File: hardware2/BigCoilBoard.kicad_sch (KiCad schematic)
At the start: 138 parts, among them J1 Conn_01x02, J10 PFC_OUT, J11 THERM2_IN, J12 THERM3_IN, J13 THERM4_IN, J14 THERM5_IN, J15 Conn_01x03, J16 Conn_ARM_JTAG_SWD_10, J17 Conn_01x04, J18 Conn_01x04, J19 Conn_01x04, J2 Conn_01x02, J20 Screw_Terminal_01x01, J21 Screw_Terminal_01x01, J22 Screw_Terminal_01x01, J23 Screw_Terminal_01x01, J3 Conn_01x03_Pin, J5 THERM1_IN, J6 Conn_01x03_Pin, J7 Conn_01x04, J8 CONTACTOR_1, J9 CONTACTOR_2, K1 G5NB-1A-DC24, K2 G5NB-1A-DC24, Q1 T2N7002AK, Q2 T2N7002AK, Q3 T2N7002AK, Q4 T2N7002AK, Q5 T2N7002AK, Q6 T2N7002AK, Q7 T2N7002AK, U1 STM32G474CBTx, U10 IF-D95, U11 IF-E96E, U12 LD1117S33TR_SOT223, U13 TC7662Bx0A, U14 L7812, U2 MCP6477-E/SN, U3 CSTNE8M00G550000R0, U4 MCP3208, U6 MGJ2D241709SC, U7 STGAP2SM, U8 SN74LV1T34DBV, U9 IF-D95

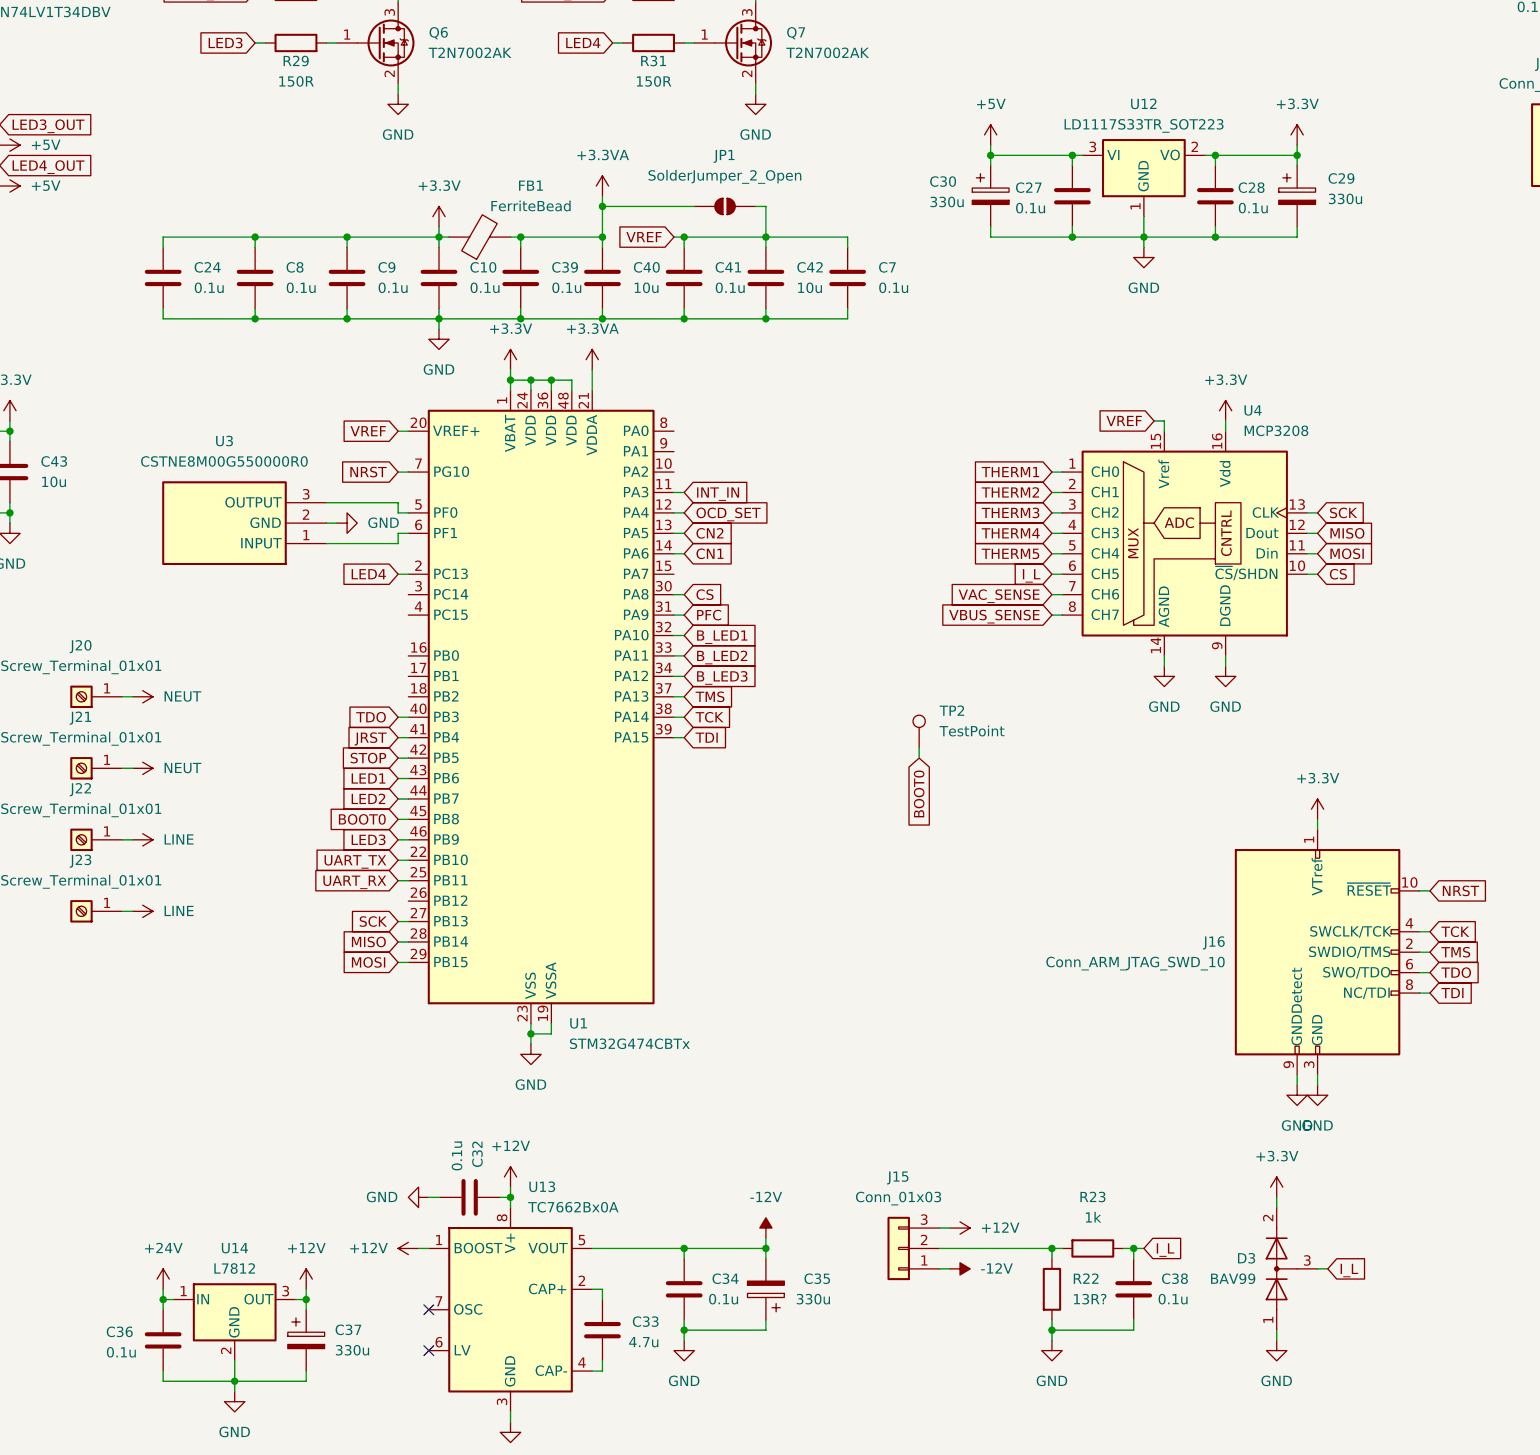
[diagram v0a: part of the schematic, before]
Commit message: back to int adc
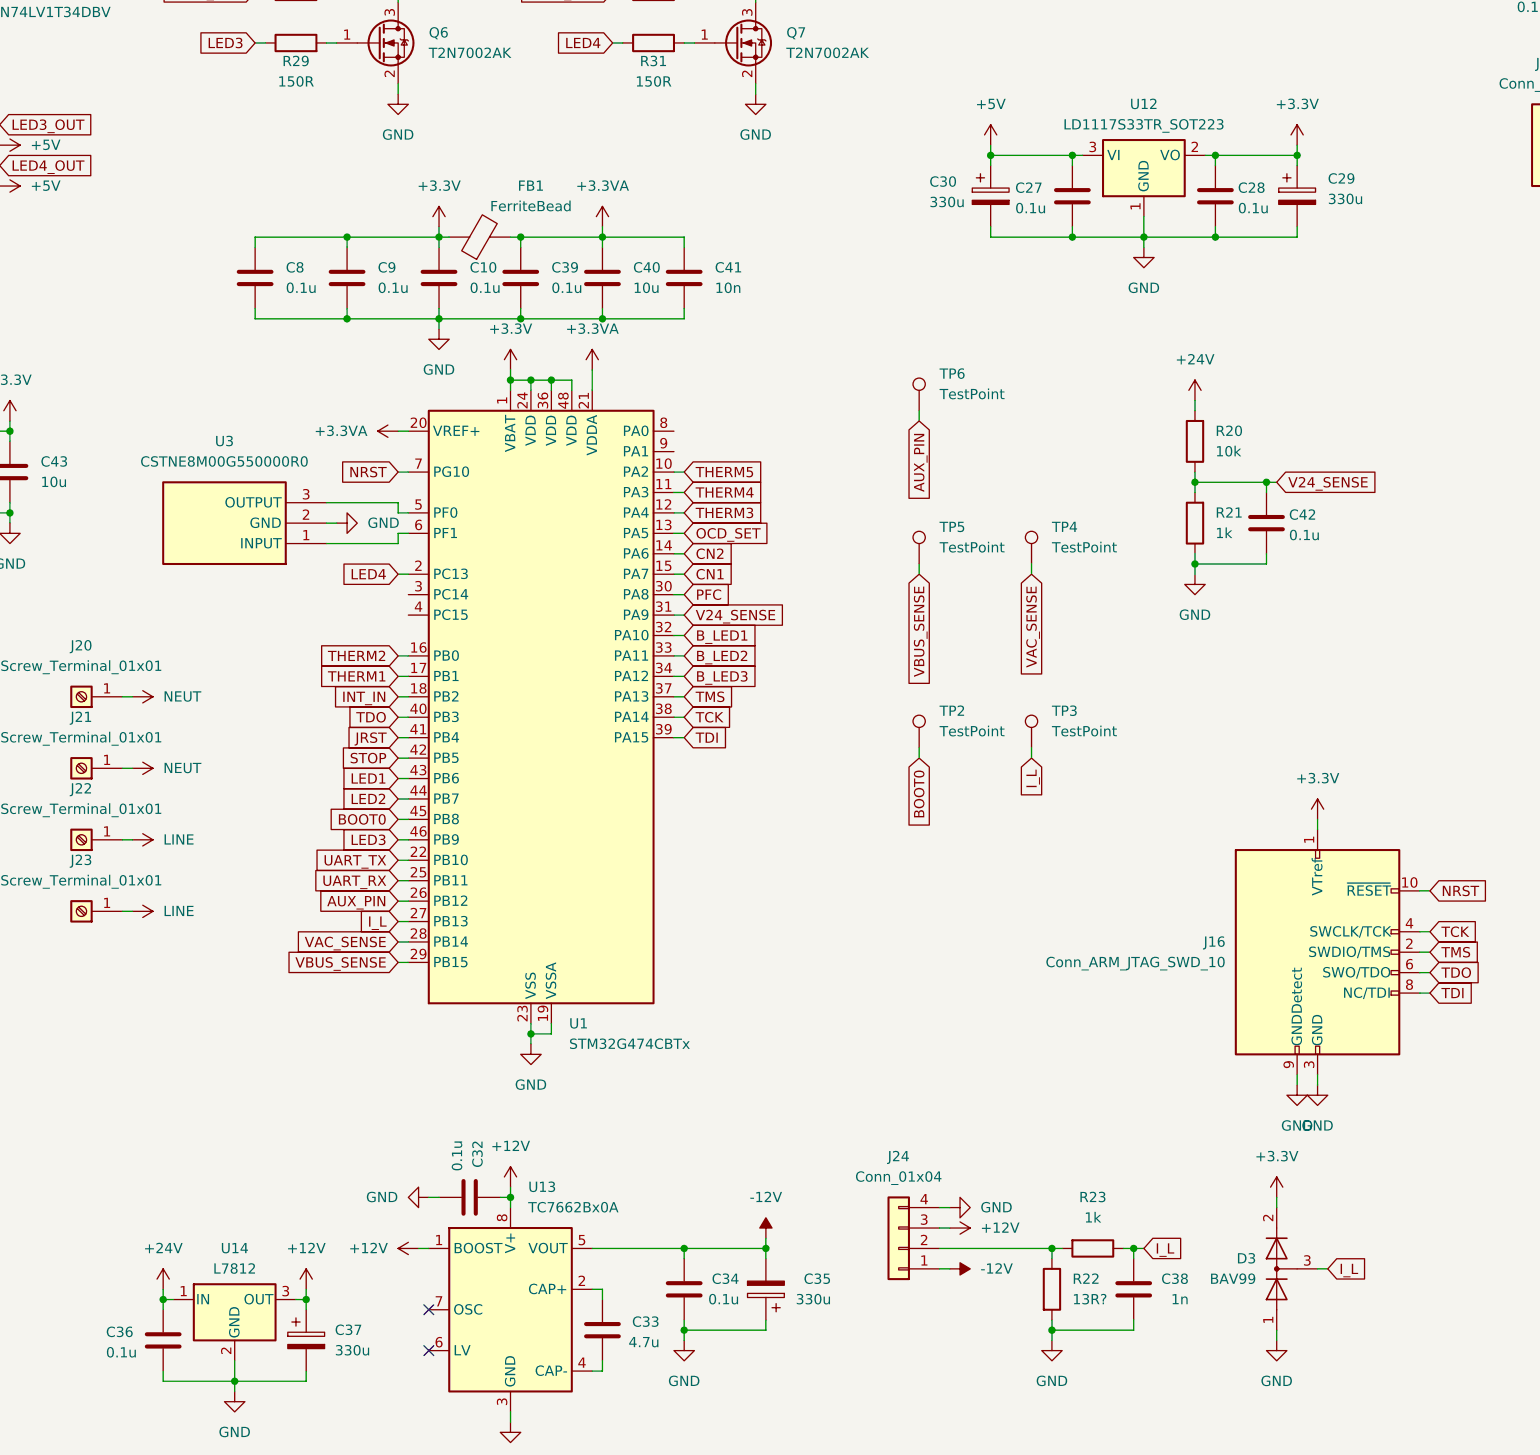
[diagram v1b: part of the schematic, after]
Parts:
- removed C24, C7: 0.1u, Capacitor_SMD:C_0805_2012Metric, symbol Device:C
- removed J15: Conn_01x03, Connector_Molex:Molex_KK-254_AE-6410-03A_1x03_P2.54mm_Vertical, symbol Connector_Generic:Conn_01x03
- removed JP1: SolderJumper_2_Open, Jumper:SolderJumper-2_P1.3mm_Open_Pad1.0x1.5mm, symbol Jumper:SolderJumper_2_Open
- removed U4: MCP3208, Package_SO:SOIC-16_3.9x9.9mm_P1.27mm, symbol Analog_ADC:MCP3208
- added J24: Conn_01x04, Connector_Molex:Molex_KK-254_AE-6410-04A_1x04_P2.54mm_Vertical, symbol Connector_Generic:Conn_01x04
- added R20: 10k, Resistor_SMD:R_0805_2012Metric, symbol Device:R
- added R21: 1k, Resistor_SMD:R_0805_2012Metric, symbol Device:R
- added TP3, TP4, TP5, TP6: TestPoint, TestPoint:TestPoint_Pad_2.0x2.0mm, symbol Connector:TestPoint
- C38: value 0.1u -> 1n
- C41: value 0.1u -> 10n
- C42: value 10u -> 0.1u
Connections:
- net CS is gone; now on net PFC: U1.30 (PA8)
- net MISO is gone; now on net VAC_SENSE: U1.28 (PB14)
- net MOSI is gone; now on net VBUS_SENSE: U1.29 (PB15)
- net SCK is gone; now on net I_L: U1.27 (PB13)
- net +12V: now also J24.3 (Pin_3)
- net +24V: now also R20.2
- net +3.3VA: now also C41.1, U1.20 (VREF+)
- net -12V: now also J24.1 (Pin_1)
- net CN1: now also U1.15 (PA7); no longer U1.14 (PA6)
- net CN2: now also U1.14 (PA6); no longer U1.13 (PA5)
- net GND: now also J24.4 (Pin_4), R21.1
- net INT_IN: now also U1.18 (PB2); no longer U1.11 (PA3)
- net I_L: now also TP3.1
- net OCD_SET: now also U1.13 (PA5); no longer U1.12 (PA4)
- net PFC: no longer U1.31 (PA9)
- net THERM1: now also U1.17 (PB1)
- net THERM2: now also U1.16 (PB0)
- net THERM3: now also U1.12 (PA4)
- net THERM4: now also U1.11 (PA3)
- net THERM5: now also U1.10 (PA2)
- net VAC_SENSE: now also TP4.1
- net VBUS_SENSE: now also TP5.1
- net at R22.1, R23.2: now also J24.2 (Pin_2)
- net AUX_PIN: now reaches U1.26 (PB12)
- net AUX_PIN: now also TP6.1
- removed net VREF: C41.1, C42.1, U1.20 (VREF+)
- new net V24_SENSE: C42.1, R20.1, R21.2, U1.31 (PA9)

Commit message: idk
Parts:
- added U5: STM32G473RCTx, Package_QFP:LQFP-64_10x10mm_P0.5mm, symbol MCU_ST_STM32G4:STM32G473RCTx
- added Y1: Resonator, Crystal:Resonator_SMD_Murata_CSTxExxV-3Pin_3.0x1.1mm, symbol Device:Resonator
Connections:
- net GND: now also Y1.2
- new net: U5.15 (VSS), U5.31 (VSS), U5.47 (VSS), U5.63 (VSS)
- new net: U5.5 (PF0), Y1.1
- new net: U5.6 (PF1), Y1.3
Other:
- note added: "use ACS772ECB-400B-PFF-T"
